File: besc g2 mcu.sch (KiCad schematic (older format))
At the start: 37 parts, among them U7 SN74LVC1G04, U8 STM32F405RGTx, Y1 Crystal

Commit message: finished routing
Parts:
- removed FB6: Ferrite_Bead_Small, Inductor_SMD:L_0603_1608Metric, symbol Device:Ferrite_Bead_Small
- C63: value C_Small -> 100n
- Y1: value Crystal -> MCSJK-7I-8.00-18-10-60-B-10
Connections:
- net +3V3: now also C62.1, C64.1, C68.1, C69.1, C70.1, C71.1, C75.1, C77.1, C79.1, C80.1, U8.1 (VBAT), U8.19 (VDD), U8.32 (VDD), U8.48 (VDD), U8.64 (VDD)
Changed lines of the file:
@@
 P 4900 3700
 F 0 "Y1" V 4854 3831 50  0000 L CNN
-F 1 "Crystal" V 4945 3831 50  0000 L CNN
+F 1 "MCSJK-7I-8.00-18-10-60-B-10" V 4945 3831 50  0001 L CNN
 F 2 "Crystal:Crystal_SMD_3225-4Pin_3.2x2.5mm" H 4900 3700 50  0001 C CNN
 F 3 "~" H 4900 3700 50  0001 C CNN
@@
 $EndComp
 $Comp
-L Device:Ferrite_Bead_Small FB6
-U 1 1 5CA1F0E0
-P 2300 1600
-F 0 "FB6" V 2350 1700 50  0000 C CNN
-F 1 "Ferrite_Bead_Small" V 2150 2050 50  0000 C CNN
-F 2 "Inductor_SMD:L_0603_1608Metric" V 2230 1600 50  0001 C CNN
-F 3 "~" H 2300 1600 50  0001 C CNN
-	1    2300 1600
-	0    1    1    0
-$EndComp
-$Comp
 L Device:Ferrite_Bead_Small FB7
 U 1 1 5CA2094F
@@
 Wire Wire Line
 	4000 1650 4000 1600
-Wire Wire Line
-	2400 1600 2600 1600
 Connection ~ 4000 1600
 Wire Wire Line
@@
 L power:+3.3V #PWR?
 U 1 1 5CAA1964
-P 2150 1550
+P 2350 1550
 AR Path="/5C9CD837/5CAA1964" Ref="#PWR?"  Part="1"
 AR Path="/5CA11DF8/5CAA1964" Ref="#PWR076"  Part="1"
-F 0 "#PWR076" H 2150 1400 50  0001 C CNN
-F 1 "+3.3V" H 2165 1723 50  0000 C CNN
-F 2 "" H 2150 1550 50  0001 C CNN
-F 3 "" H 2150 1550 50  0001 C CNN
-	1    2150 1550
-	1    0    0    -1
-$EndComp
-Wire Wire Line
-	2150 1550 2150 1600
-Wire Wire Line
-	2200 1600 2150 1600
+F 0 "#PWR076" H 2350 1400 50  0001 C CNN
+F 1 "+3.3V" H 2365 1723 50  0000 C CNN
+F 2 "" H 2350 1550 50  0001 C CNN
+F 3 "" H 2350 1550 50  0001 C CNN
+	1    2350 1550
+	1    0    0    -1
+$EndComp
+Wire Wire Line
+	2350 1550 2350 1600
 $Comp
 L Device:C_Small C81
@@
 P 2650 5600
 F 0 "C63" H 2742 5646 50  0000 L CNN
-F 1 "C_Small" H 2742 5555 50  0000 L CNN
+F 1 "100n" H 2742 5555 50  0000 L CNN
 F 2 "Capacitor_SMD:C_0603_1608Metric" H 2650 5600 50  0001 C CNN
 F 3 "~" H 2650 5600 50  0001 C CNN
@@
 Wire Wire Line
 	4650 2300 4650 2250
+Wire Wire Line
+	2350 1600 2600 1600
 $EndSCHEMATC

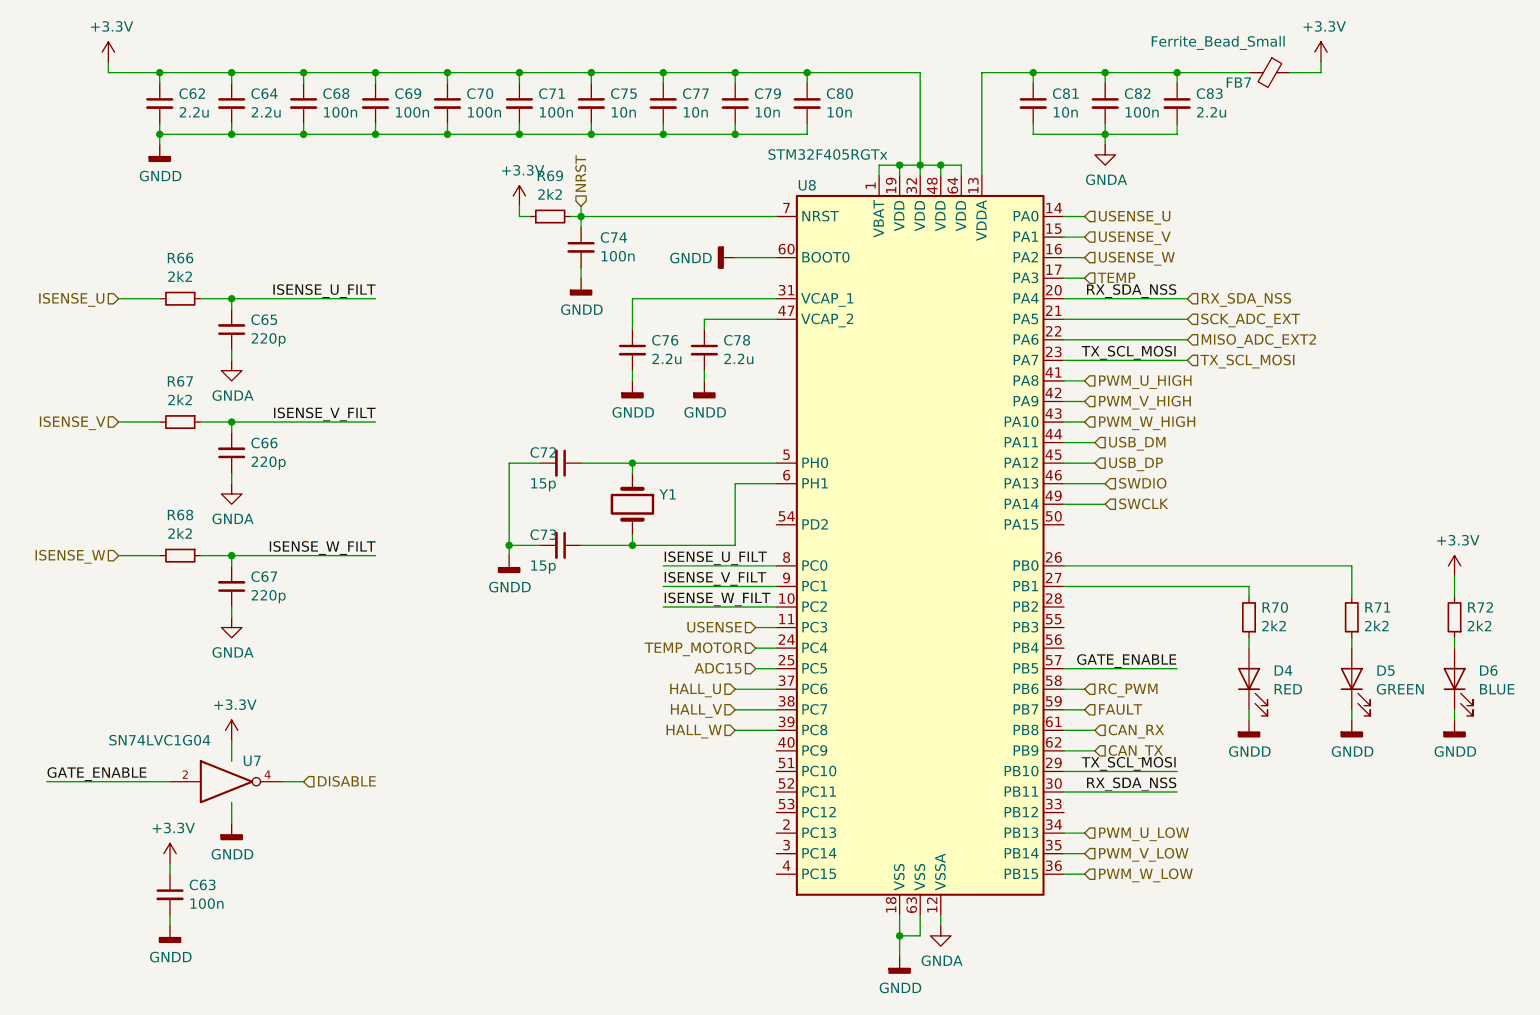
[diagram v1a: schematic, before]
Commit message: finished routing, added bom and step
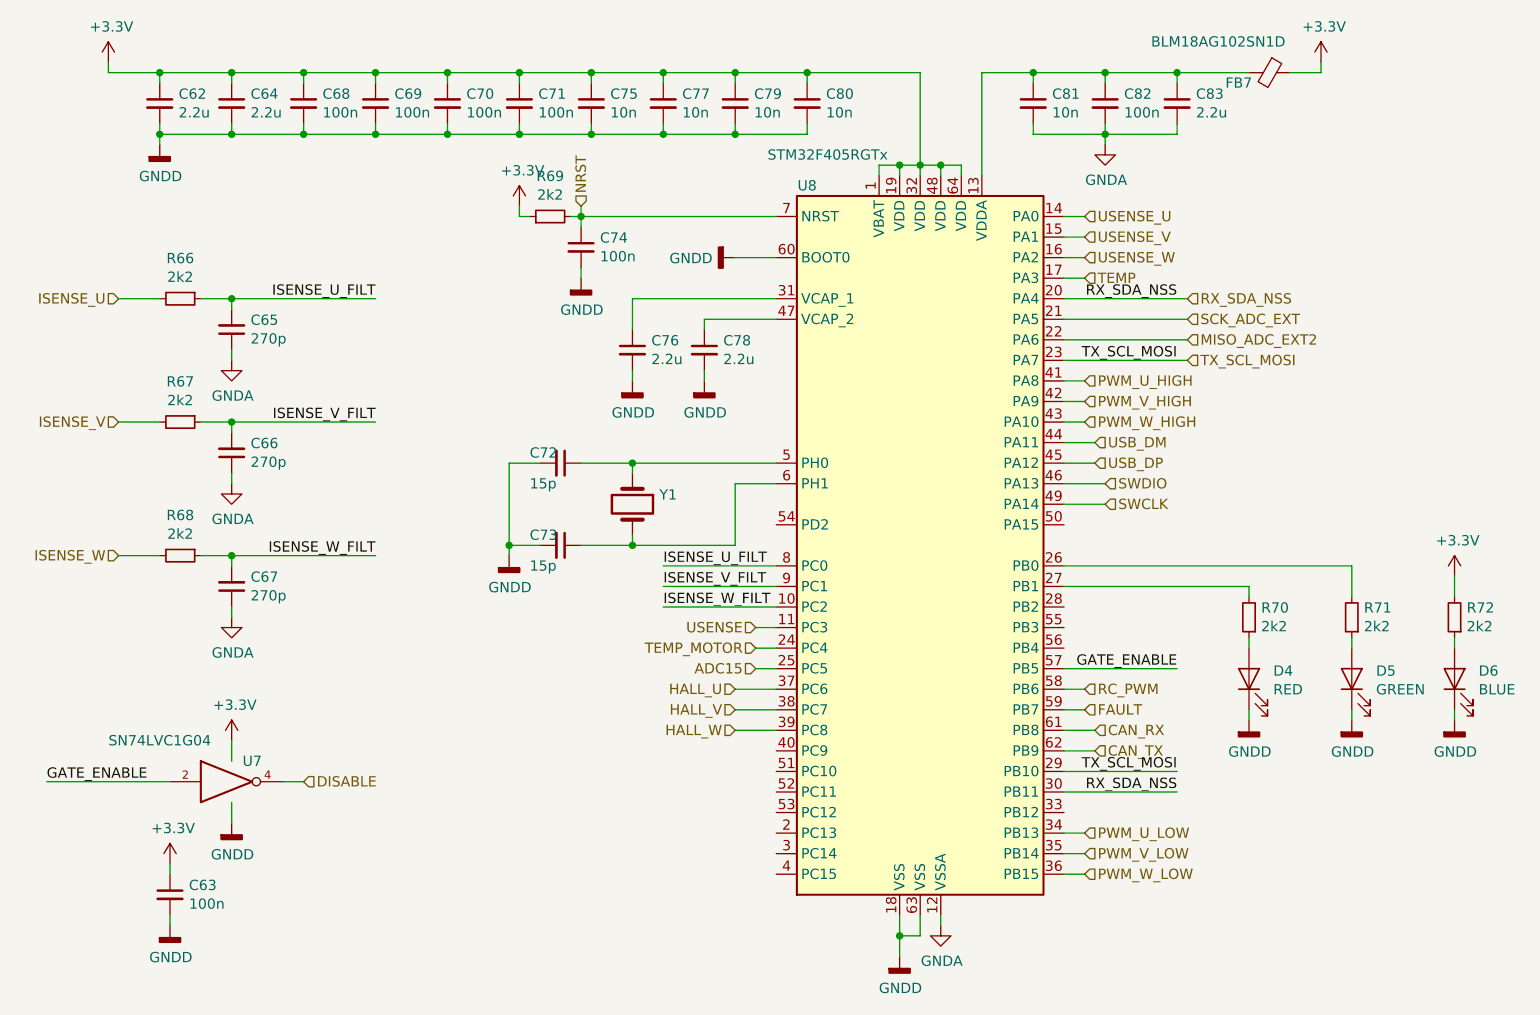
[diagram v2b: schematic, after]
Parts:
- C65, C66, C67: value 220p -> 270p
- FB7: value Ferrite_Bead_Small -> BLM18AG102SN1D
- Y1: footprint Crystal:Crystal_SMD_3225-4Pin_3.2x2.5mm -> Crystal:Crystal_SMD_5032-4Pin_5.0x3.2mm
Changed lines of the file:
@@
 encoding utf-8
 Sheet 3 5
-Title ""
-Date ""
-Rev ""
-Comp ""
+Title "BESC Gen 2"
+Date "14.7.2019"
+Rev "init"
+Comp "e.pavlin.si"
 Comment1 ""
 Comment2 ""
@@
 F 0 "Y1" V 4854 3831 50  0000 L CNN
 F 1 "MCSJK-7I-8.00-18-10-60-B-10" V 4945 3831 50  0001 L CNN
-F 2 "Crystal:Crystal_SMD_3225-4Pin_3.2x2.5mm" H 4900 3700 50  0001 C CNN
+F 2 "Crystal:Crystal_SMD_5032-4Pin_5.0x3.2mm" H 4900 3700 50  0001 C CNN
 F 3 "~" H 4900 3700 50  0001 C CNN
 	1    4900 3700
@@
 P 8000 1600
 F 0 "FB7" V 8050 1450 50  0000 C CNN
-F 1 "Ferrite_Bead_Small" V 7850 1350 50  0000 C CNN
+F 1 "BLM18AG102SN1D" V 7850 1350 50  0000 C CNN
 F 2 "Inductor_SMD:L_0603_1608Metric" V 7930 1600 50  0001 C CNN
 F 3 "~" H 8000 1600 50  0001 C CNN
@@
 P 2950 2850
 F 0 "C65" H 2858 2804 50  0000 R CNN
-F 1 "220p" H 2858 2895 50  0000 R CNN
+F 1 "270p" H 2858 2895 50  0000 R CNN
 F 2 "Capacitor_SMD:C_0603_1608Metric" H 2950 2850 50  0001 C CNN
 F 3 "~" H 2950 2850 50  0001 C CNN
@@
 P 2950 3450
 F 0 "C66" H 2858 3404 50  0000 R CNN
-F 1 "220p" H 2858 3495 50  0000 R CNN
+F 1 "270p" H 2858 3495 50  0000 R CNN
 F 2 "Capacitor_SMD:C_0603_1608Metric" H 2950 3450 50  0001 C CNN
 F 3 "~" H 2950 3450 50  0001 C CNN
@@
 P 2950 4100
 F 0 "C67" H 2858 4054 50  0000 R CNN
-F 1 "220p" H 2858 4145 50  0000 R CNN
+F 1 "270p" H 2858 4145 50  0000 R CNN
 F 2 "Capacitor_SMD:C_0603_1608Metric" H 2950 4100 50  0001 C CNN
 F 3 "~" H 2950 4100 50  0001 C CNN

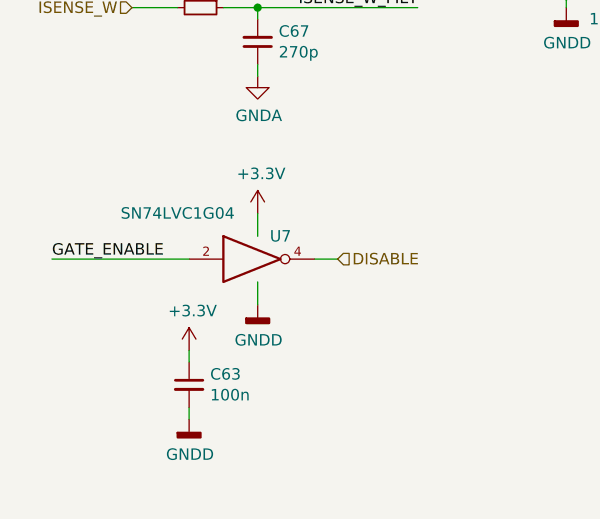
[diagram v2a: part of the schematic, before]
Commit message: removed inverter for gate enable, fixed bugs on pcb
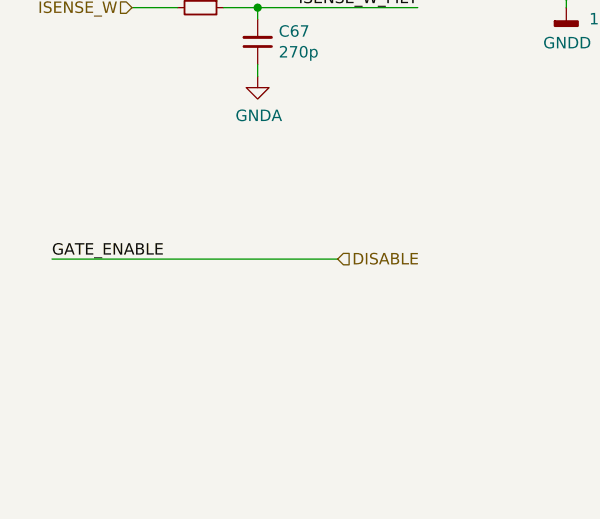
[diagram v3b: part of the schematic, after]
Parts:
- removed C63: 100n, Capacitor_SMD:C_0603_1608Metric, symbol Device:C_Small
- removed U7: SN74LVC1G04, Package_TO_SOT_SMD:SOT-23-5, symbol 74xGxx:74AHC1G04
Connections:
- net GATE_ENABLE is gone; now on net DISABLE: U8.57 (PB5)
- net GND renamed GNDD
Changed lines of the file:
@@
 	8250 1600 8250 1550
-$Comp
-L 74xGxx:74AHC1G04 U7
-U 1 1 5CEB8C8A
-P 2950 5050
-F 0 "U7" H 3050 5150 50  0000 C CNN
-F 1 "SN74LVC1G04" H 2600 5250 50  0000 C CNN
-F 2 "Package_TO_SOT_SMD:SOT-23-5" H 2950 5050 50  0001 C CNN
-F 3 "http://www.ti.com/lit/sg/scyt129e/scyt129e.pdf" H 2950 5050 50  0001 C CNN
-	1    2950 5050
-	1    0    0    -1
-$EndComp
-$Comp
-L power:GNDD #PWR084
-U 1 1 5CEB9CDA
-P 2950 5250
-F 0 "#PWR084" H 2950 5000 50  0001 C CNN
-F 1 "GNDD" H 2954 5095 50  0000 C CNN
-F 2 "" H 2950 5250 50  0001 C CNN
-F 3 "" H 2950 5250 50  0001 C CNN
-	1    2950 5250
-	1    0    0    -1
-$EndComp
-Wire Wire Line
-	2950 5150 2950 5250
-$Comp
-L power:+3.3V #PWR?
-U 1 1 5CEBBABE
-P 2950 4850
-AR Path="/5C9CD837/5CEBBABE" Ref="#PWR?"  Part="1"
-AR Path="/5CA11DF8/5CEBBABE" Ref="#PWR083"  Part="1"
-F 0 "#PWR083" H 2950 4700 50  0001 C CNN
-F 1 "+3.3V" H 2965 5023 50  0000 C CNN
-F 2 "" H 2950 4850 50  0001 C CNN
-F 3 "" H 2950 4850 50  0001 C CNN
-	1    2950 4850
-	1    0    0    -1
-$EndComp
-Wire Wire Line
-	2950 4950 2950 4850
-$Comp
-L Device:C_Small C63
-U 1 1 5CEBE2DF
-P 2650 5600
-F 0 "C63" H 2742 5646 50  0000 L CNN
-F 1 "100n" H 2742 5555 50  0000 L CNN
-F 2 "Capacitor_SMD:C_0603_1608Metric" H 2650 5600 50  0001 C CNN
-F 3 "~" H 2650 5600 50  0001 C CNN
-	1    2650 5600
-	1    0    0    -1
-$EndComp
-$Comp
-L power:+3.3V #PWR?
-U 1 1 5CEC2304
-P 2650 5450
-AR Path="/5C9CD837/5CEC2304" Ref="#PWR?"  Part="1"
-AR Path="/5CA11DF8/5CEC2304" Ref="#PWR078"  Part="1"
-F 0 "#PWR078" H 2650 5300 50  0001 C CNN
-F 1 "+3.3V" H 2665 5623 50  0000 C CNN
-F 2 "" H 2650 5450 50  0001 C CNN
-F 3 "" H 2650 5450 50  0001 C CNN
-	1    2650 5450
-	1    0    0    -1
-$EndComp
-$Comp
-L power:GNDD #PWR079
-U 1 1 5CEC41E9
-P 2650 5750
-F 0 "#PWR079" H 2650 5500 50  0001 C CNN
-F 1 "GNDD" H 2654 5595 50  0000 C CNN
-F 2 "" H 2650 5750 50  0001 C CNN
-F 3 "" H 2650 5750 50  0001 C CNN
-	1    2650 5750
-	1    0    0    -1
-$EndComp
-Wire Wire Line
-	2650 5450 2650 5500
-Wire Wire Line
-	2650 5700 2650 5750
-Wire Wire Line
-	3200 5050 3300 5050
 $Comp
 L Device:C_Small C65
@@
 Text Label 2050 5050 0    50   ~ 0
 GATE_ENABLE
-Wire Wire Line
-	2650 5050 2050 5050
 Text HLabel 7100 4600 2    50   Input ~ 0
 RC_PWM
@@
 Wire Wire Line
 	2350 1600 2600 1600
+Wire Wire Line
+	2050 5050 3300 5050
 $EndSCHEMATC
